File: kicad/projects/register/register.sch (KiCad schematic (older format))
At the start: 23 parts, among them U3 74HCT04

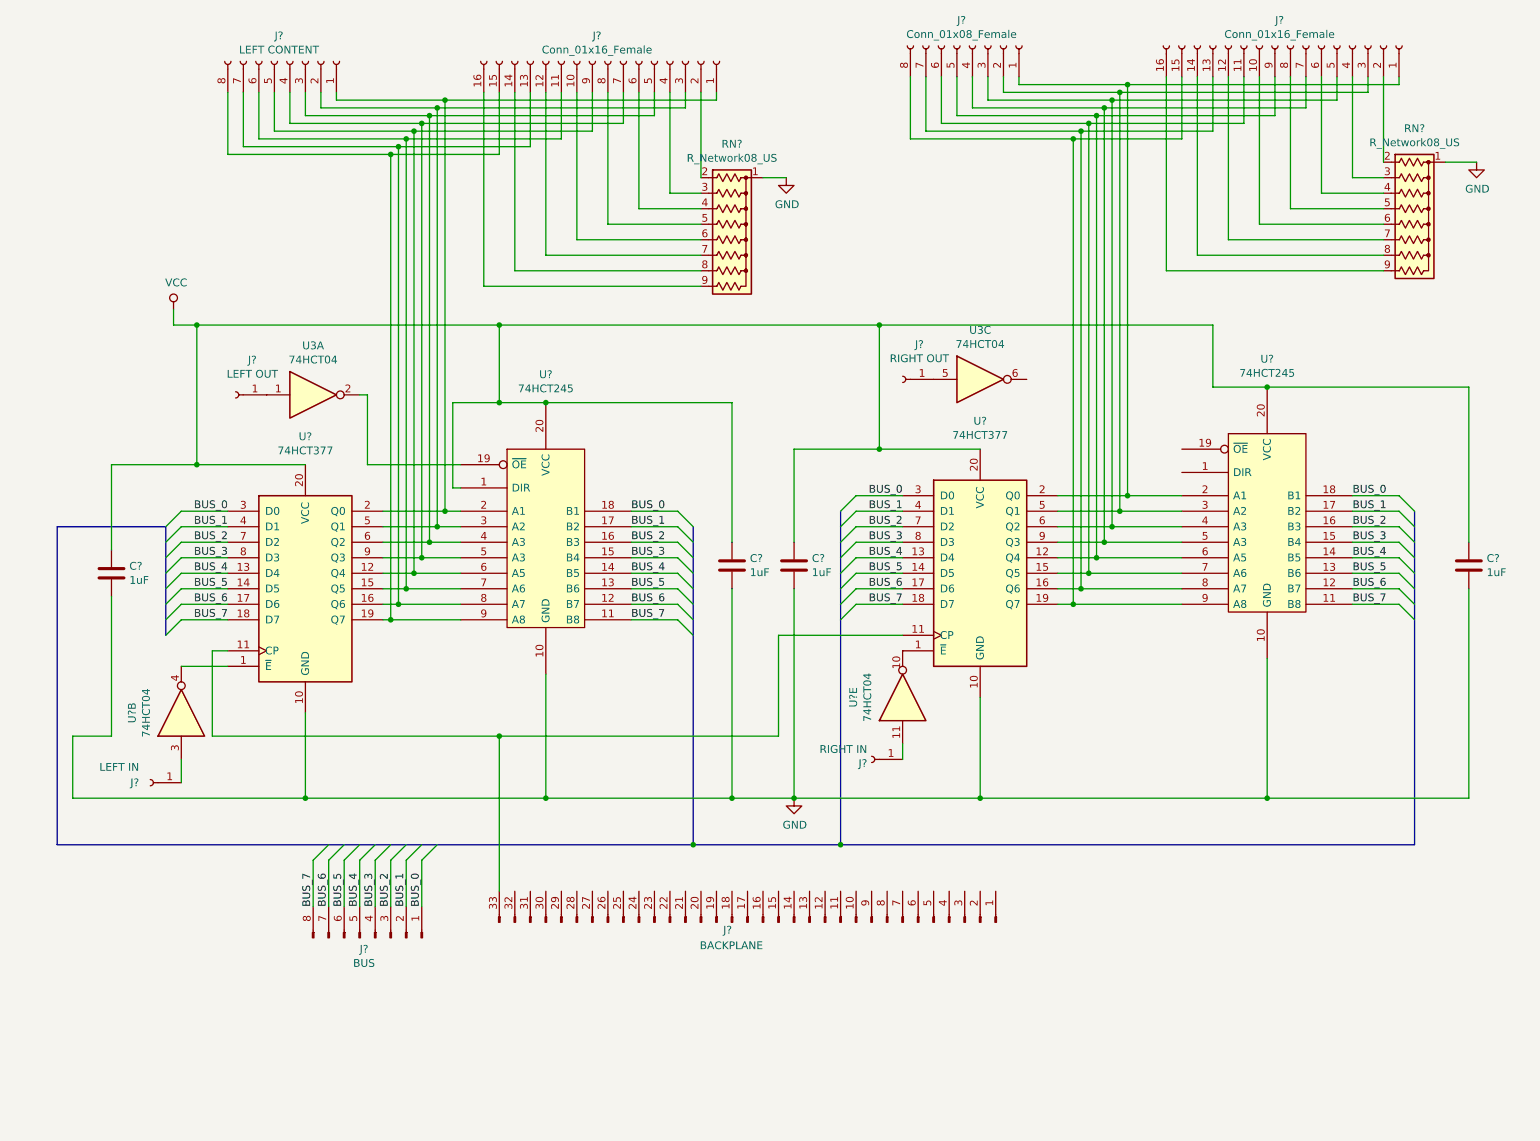
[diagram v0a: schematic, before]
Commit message: Start making PCB for register.
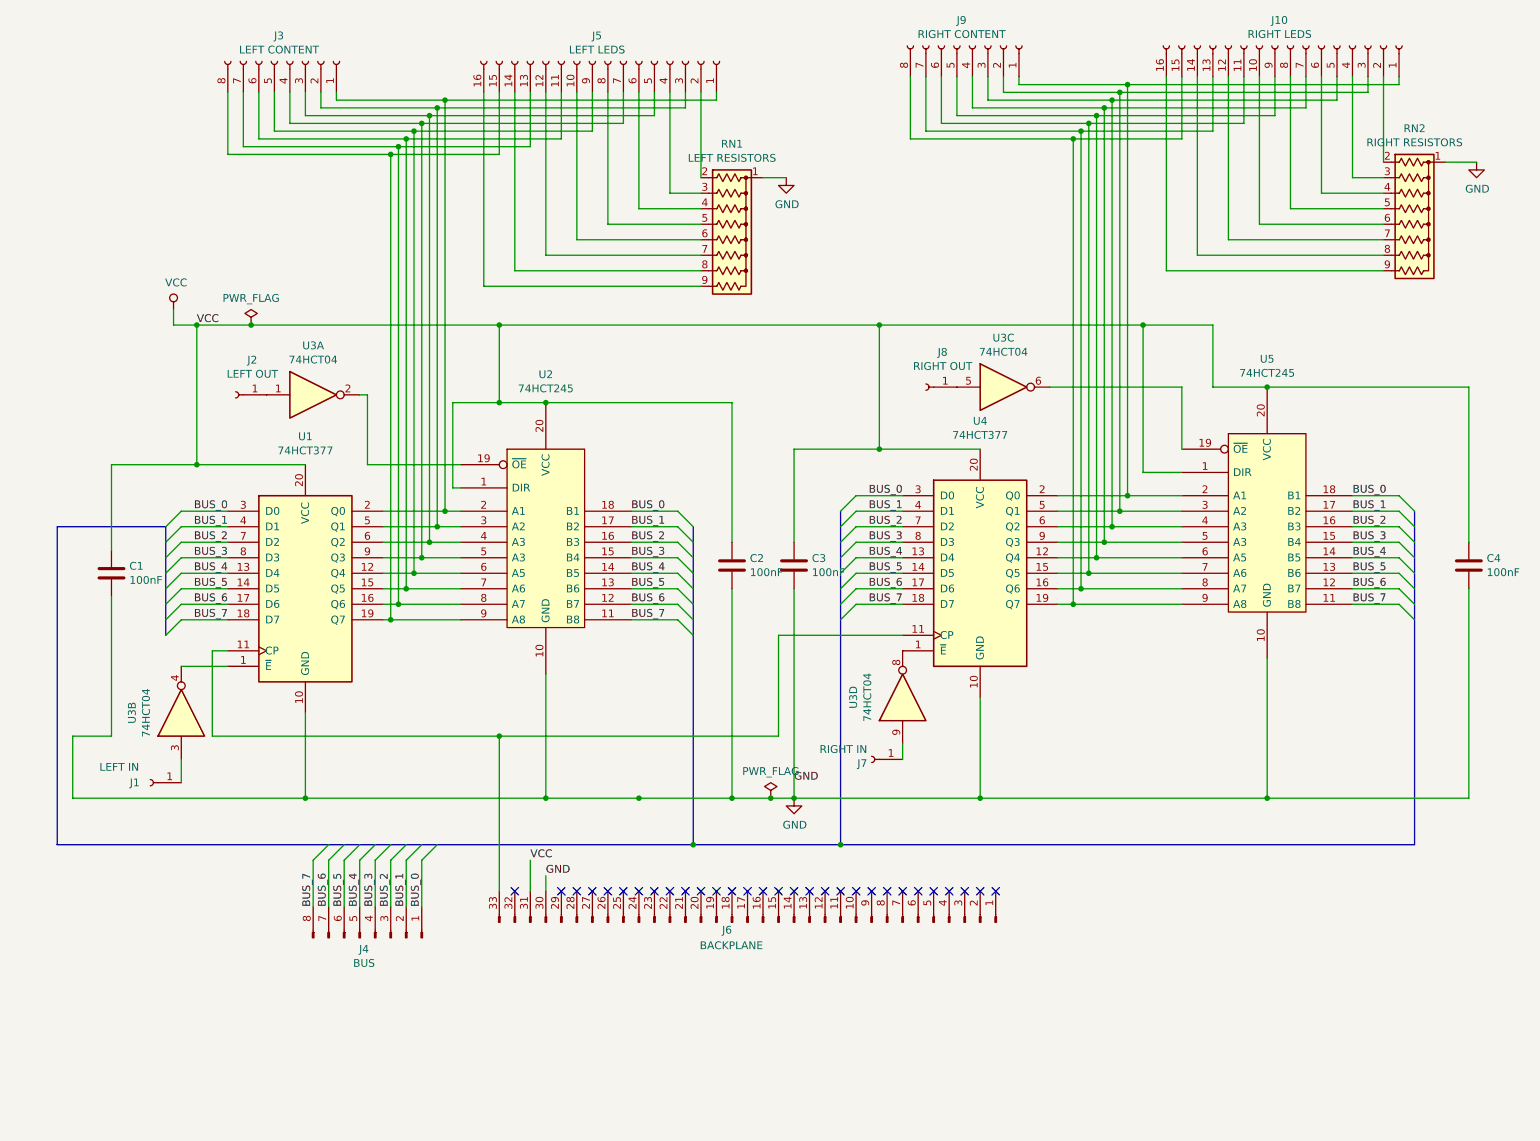
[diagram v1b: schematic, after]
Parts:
- C1, C2, C3, C4: renamed from C?; value 1uF -> 100nF; footprint (none) -> Capacitor_THT:C_Disc_D4.7mm_W2.5mm_P5.00mm
- J1, J2, J7, J8: renamed from J?; footprint (none) -> Connector_Wire:SolderWirePad_1x01_Drill1mm
- J10: renamed from J?; value Conn_01x16_Female -> RIGHT LEDS; footprint (none) -> Connector_PinSocket_2.54mm:PinSocket_1x16_P2.54mm_Horizontal
- J3: renamed from J?; footprint (none) -> Connector_PinSocket_2.54mm:PinSocket_1x08_P2.54mm_Horizontal
- J4: renamed from J?; footprint (none) -> Connector_PinHeader_2.54mm:PinHeader_1x08_P2.54mm_Horizontal
- J5: renamed from J?; value Conn_01x16_Female -> LEFT LEDS; footprint (none) -> Connector_PinSocket_2.54mm:PinSocket_1x16_P2.54mm_Horizontal
- J6: renamed from J?; footprint (none) -> Connector_PinHeader_2.54mm:PinHeader_1x34_P2.54mm_Horizontal
- J9: renamed from J?; value Conn_01x08_Female -> RIGHT CONTENT; footprint (none) -> Connector_PinSocket_2.54mm:PinSocket_1x08_P2.54mm_Horizontal
- RN1: renamed from RN?; value R_Network08_US -> LEFT RESISTORS
- RN2: renamed from RN?; value R_Network08_US -> RIGHT RESISTORS
- U1, U2, U4, U5: renamed from U?; footprint (none) -> Package_DIP:DIP-20_W7.62mm_Socket
- gave numbers to parts that had none: 1
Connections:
- net GND: now also J6.30 (Pin_30)
- net VCC: now also J6.31 (Pin_31), U5.1 (DIR)
- net at U3.6: now also U5.19 (~OE)
- net at J7.1 (Pin_1): now also U3.9; no longer U3.11
- net at U4.1 (~E): now also U3.8; no longer U3.10
- no-connect marks 0 -> 30
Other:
- moved on the sheet: J8, U3C

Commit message: Add start of control unit in kicad. Start routing register PCB, need to make traces thinner...
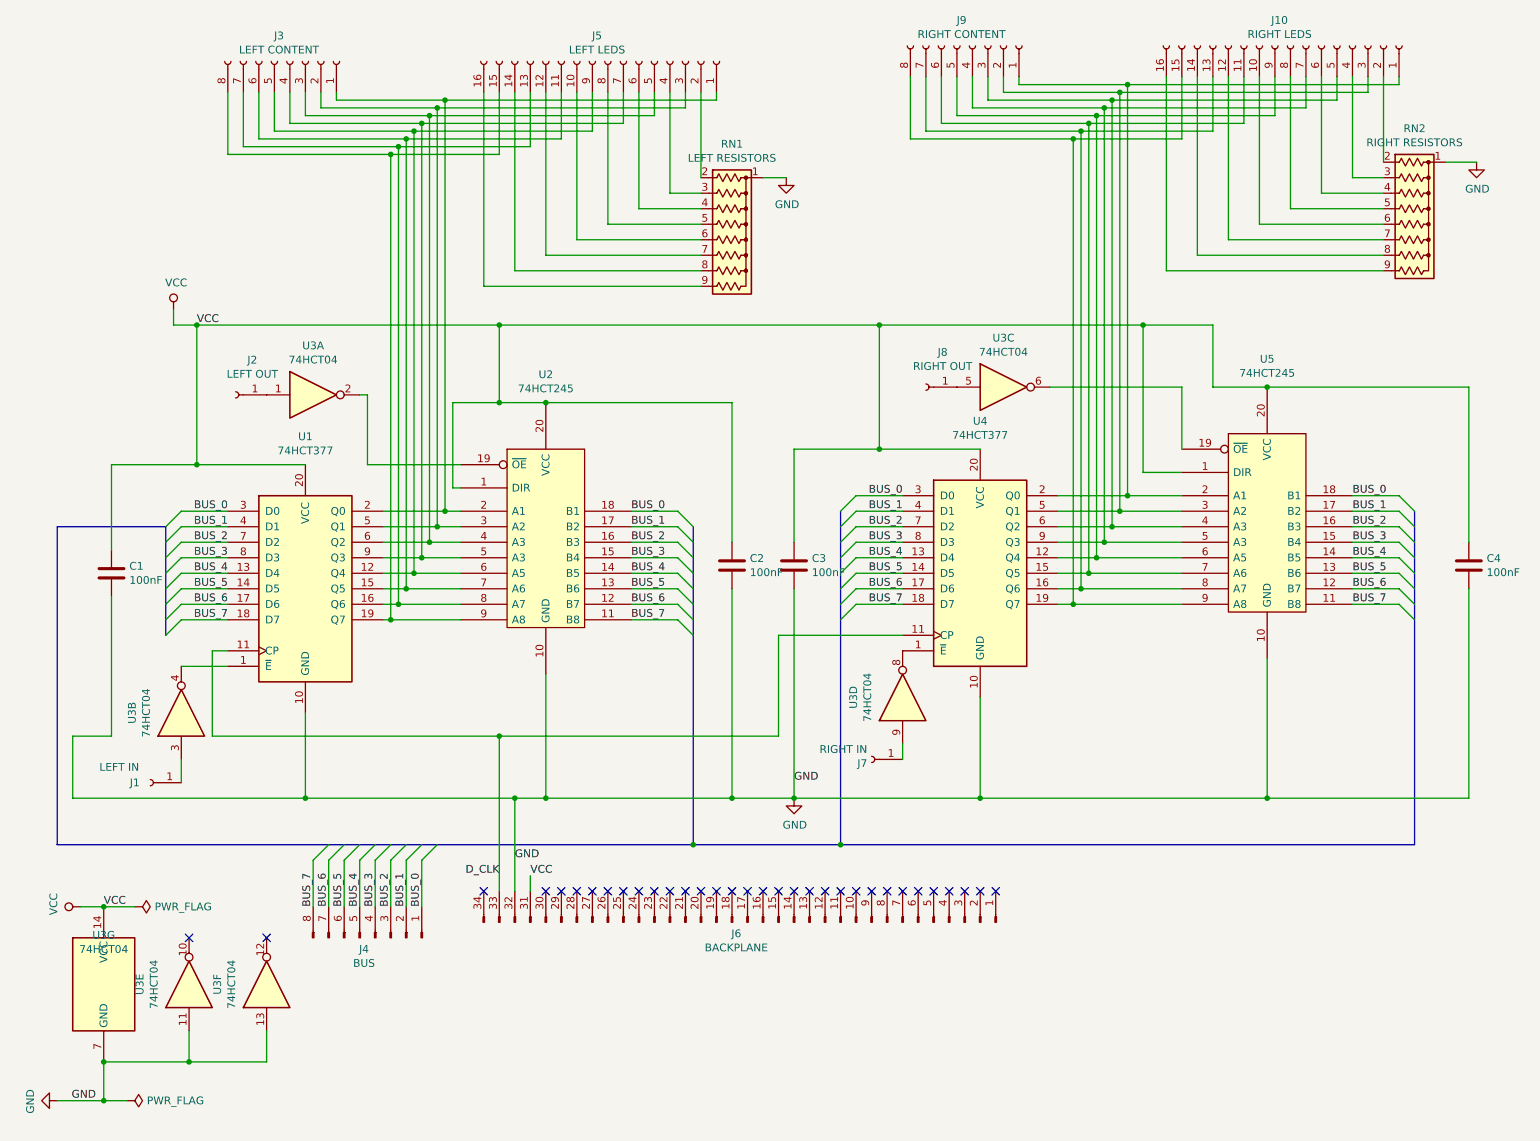
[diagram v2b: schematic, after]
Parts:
- removed J6: BACKPLANE, Connector_PinHeader_2.54mm:PinHeader_1x34_P2.54mm_Horizontal, symbol Connector:Conn_01x33_Male
- added J6: BACKPLANE, eight-bit-computer:backplane-connector, symbol Connector:Conn_01x34_Male
- added unit 7 of U3
- added unit 5 of U3
- added unit 6 of U3
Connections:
- net GND: now also J6.32 (Pin_32), U3.11, U3.13, U3.7 (GND)
- net VCC: now also J6.31 (Pin_31), U3.14 (VCC)
- net D_CLK: now reaches U1.11 (CP), U4.11 (CP)
- net D_CLK: now also J6.33 (Pin_33)
- no-connect marks 30 -> 33
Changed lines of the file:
@@
-$EndComp
-$Comp
-L Connector:Conn_01x33_Male J6
-U 1 1 5E1828CF
-P 5300 6650
-F 0 "J6" V 5250 6550 50  0000 R CNN
-F 1 "BACKPLANE" V 5150 6750 50  0000 R CNN
-F 2 "Connector_PinHeader_2.54mm:PinHeader_1x34_P2.54mm_Horizontal" H 5300 6650 50  0001 C CNN
-F 3 "~" H 5300 6650 50  0001 C CNN
-	1    5300 6650
-	0    1    -1   0
 $EndComp
 $Comp
@@
 	2900 6550 2900 6250
 Wire Wire Line
-	2800 6550 2800 6250
-Wire Wire Line
 	2700 6550 2700 6250
 Wire Wire Line
@@
 Connection ~ 6150 2800
 Wire Wire Line
-	1750 2800 2100 2800
-Wire Wire Line
 	3700 3300 3700 2800
 Connection ~ 3700 3300
@@
 	9800 1750 10000 1750
 Wire Wire Line
-	3700 6450 3700 5450
-Wire Wire Line
 	1850 4900 1950 4900
 Connection ~ 3700 5450
@@
 	2450 5300 2450 5850
 Wire Wire Line
-	2450 5850 4000 5850
+	2450 5850 3800 5850
 Wire Wire Line
 	8650 5850 8650 4950
@@
 	5200 4500 5200 5850
 Connection ~ 5200 5850
-Wire Wire Line
-	5200 5850 5450 5850
 Wire Wire Line
 	9950 3200 9950 4200
@@
 Wire Wire Line
 	8100 3200 8100 3600
-NoConn ~ 3800 6450
 NoConn ~ 4100 6450
 NoConn ~ 4200 6450
@@
 Text Label 1750 2800 0    50   ~ 0
 VCC
-Text Label 3900 6250 0    50   ~ 0
+Text Label 3900 6350 0    50   ~ 0
 VCC
-Text Label 4000 6350 0    50   ~ 0
+Text Label 3800 6250 0    50   ~ 0
 GND
-Wire Wire Line
-	4000 5850 4600 5850
-Wire Wire Line
-	4000 6450 4000 6350
-Wire Wire Line
-	3900 6450 3900 6250
+Text Label 5600 5750 0    50   ~ 0
+GND
+$Comp
+L Connector:Conn_01x34_Male J6
+U 1 1 5E143442
+P 5300 6650
+F 0 "J6" V 5227 6578 50  0000 C CNN
+F 1 "BACKPLANE" V 5136 6578 50  0000 C CNN
+F 2 "eight-bit-computer:backplane-connector" H 5300 6650 50  0001 C CNN
+F 3 "~" H 5300 6650 50  0001 C CNN
+	1    5300 6650
+	0    1    -1   0
+$EndComp
+NoConn ~ 3600 6450
+Wire Wire Line
+	3700 5450 3700 6450
+NoConn ~ 4000 6450
+Text Label 3700 6350 2    50   ~ 0
+D_CLK
+Wire Wire Line
+	3900 6450 3900 6350
+Wire Wire Line
+	3800 5850 3800 6450
+Connection ~ 3800 5850
+Wire Wire Line
+	3800 5850 4000 5850
+$Comp
+L 74xx:74HCT04 U3
+U 7 1 5E204B57
+P 1150 7050
+F 0 "U3" H 1150 7367 50  0000 C CNN
+F 1 "74HCT04" H 1150 7276 50  0000 C CNN
+F 2 "Package_DIP:DIP-14_W7.62mm_Socket" H 1150 7050 50  0001 C CNN
+F 3 "https://assets.nexperia.com/documents/data-sheet/74HC_HCT04.pdf" H 1150 7050 50  0001 C CNN
+	7    1150 7050
+	1    0    0    -1
+$EndComp
+$Comp
+L 74xx:74HCT04 U3
+U 5 1 5E206221
+P 1700 7050
+F 0 "U3" H 1700 7367 50  0000 C CNN
+F 1 "74HCT04" H 1700 7276 50  0000 C CNN
+F 2 "Package_DIP:DIP-14_W7.62mm_Socket" H 1700 7050 50  0001 C CNN
+F 3 "https://assets.nexperia.com/documents/data-sheet/74HC_HCT04.pdf" H 1700 7050 50  0001 C CNN
+	5    1700 7050
+	0    -1   -1   0
+$EndComp
+$Comp
+L 74xx:74HCT04 U3
+U 6 1 5E2090E4
+P 2200 7050
+F 0 "U3" H 2200 7367 50  0000 C CNN
+F 1 "74HCT04" H 2200 7276 50  0000 C CNN
+F 2 "Package_DIP:DIP-14_W7.62mm_Socket" H 2200 7050 50  0001 C CNN
+F 3 "https://assets.nexperia.com/documents/data-sheet/74HC_HCT04.pdf" H 2200 7050 50  0001 C CNN
+	6    2200 7050
+	0    -1   -1   0
+$EndComp
+$Comp
+L power:VCC #PWR0103
+U 1 1 5E263592
+P 1000 6550
+F 0 "#PWR0103" H 1000 6400 50  0001 C CNN
+F 1 "VCC" H 1017 6723 50  0000 C CNN
+F 2 "" H 1000 6550 50  0001 C CNN
+F 3 "" H 1000 6550 50  0001 C CNN
+	1    1000 6550
+	0    -1   -1   0
+$EndComp
+Text Label 1150 6550 0    50   ~ 0
+VCC
+Wire Wire Line
+	1000 6550 1150 6550
+Connection ~ 1150 6550
+Wire Wire Line
+	1150 6550 1350 6550
+$Comp
+L power:GND #PWR0104
+U 1 1 5E2B420D
+P 850 7800
+F 0 "#PWR0104" H 850 7550 50  0001 C CNN
+F 1 "GND" H 855 7627 50  0000 C CNN
+F 2 "" H 850 7800 50  0001 C CNN
+F 3 "" H 850 7800 50  0001 C CNN
+	1    850  7800
+	0    1    1    0
+$EndComp
+Text Label 1100 7800 2    50   ~ 0
+GND
+Wire Wire Line
+	2800 6250 2800 6550
+Wire Wire Line
+	1150 7550 1700 7550
+Wire Wire Line
+	1700 7350 1700 7550
+Wire Wire Line
+	2200 7550 1700 7550
+Connection ~ 1700 7550
+Wire Wire Line
+	2200 7550 2200 7350
+NoConn ~ 2200 6750
+NoConn ~ 1700 6750
+Wire Wire Line
+	5200 5850 5600 5850
+Wire Wire Line
+	1750 2800 3700 2800
+Wire Wire Line
+	4000 5850 5200 5850
+$Comp
+L power:PWR_FLAG #FLG0101
+U 1 1 5E49A01D
+P 1350 6550
+F 0 "#FLG0101" H 1350 6625 50  0001 C CNN
+F 1 "PWR_FLAG" V 1350 6678 50  0000 L CNN
+F 2 "" H 1350 6550 50  0001 C CNN
+F 3 "~" H 1350 6550 50  0001 C CNN
+	1    1350 6550
+	0    1    1    0
+$EndComp
+Wire Wire Line
+	1150 7800 1300 7800
+Connection ~ 1150 7800
+Wire Wire Line
+	1150 7550 1150 7800
+Connection ~ 1150 7550
+$Comp
+L power:PWR_FLAG #FLG0102
+U 1 1 5E643EA5
+P 1300 7800
+F 0 "#FLG0102" H 1300 7875 50  0001 C CNN
+F 1 "PWR_FLAG" V 1300 7928 50  0000 L CNN
+F 2 "" H 1300 7800 50  0001 C CNN
+F 3 "~" H 1300 7800 50  0001 C CNN
+	1    1300 7800
+	0    1    1    0
+$EndComp
+Wire Wire Line
+	850  7800 1150 7800
 Wire Bus Line
 	9600 4000 9600 6150
@@
 Wire Bus Line
 	850  6150 4950 6150
-Text Label 5600 5750 0    50   ~ 0
-GND
-$Comp
-L power:PWR_FLAG #FLG0101
-U 1 1 5E3D7019
-P 2100 2800
-F 0 "#FLG0101" H 2100 2875 50  0001 C CNN
-F 1 "PWR_FLAG" H 2100 2973 50  0000 C CNN
-F 2 "" H 2100 2800 50  0001 C CNN
-F 3 "~" H 2100 2800 50  0001 C CNN
-	1    2100 2800
-	1    0    0    -1
-$EndComp
-Connection ~ 2100 2800
-Wire Wire Line
-	2100 2800 3700 2800
-$Comp
-L power:PWR_FLAG #FLG0102
-U 1 1 5E3D75BE
-P 5450 5850
-F 0 "#FLG0102" H 5450 5925 50  0001 C CNN
-F 1 "PWR_FLAG" H 5450 6023 50  0000 C CNN
-F 2 "" H 5450 5850 50  0001 C CNN
-F 3 "~" H 5450 5850 50  0001 C CNN
-	1    5450 5850
-	1    0    0    -1
-$EndComp
-Connection ~ 4600 5850
-Wire Wire Line
-	4600 5850 5200 5850
-Connection ~ 5450 5850
-Wire Wire Line
-	5450 5850 5600 5850
 $EndSCHEMATC
